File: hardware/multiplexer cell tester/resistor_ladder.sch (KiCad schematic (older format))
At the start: 27 parts, among them U10 ADG841YKSZ-500RL7, U11 ADG841YKSZ-500RL7, U12 ADG841YKSZ-500RL7, U13 74HC590, U13 ADG841YKSZ-500RL7, U6 ADG841YKSZ-500RL7, U7 ADG841YKSZ-500RL7, U8 ADG841YKSZ-500RL7, U9 ADG841YKSZ-500RL7

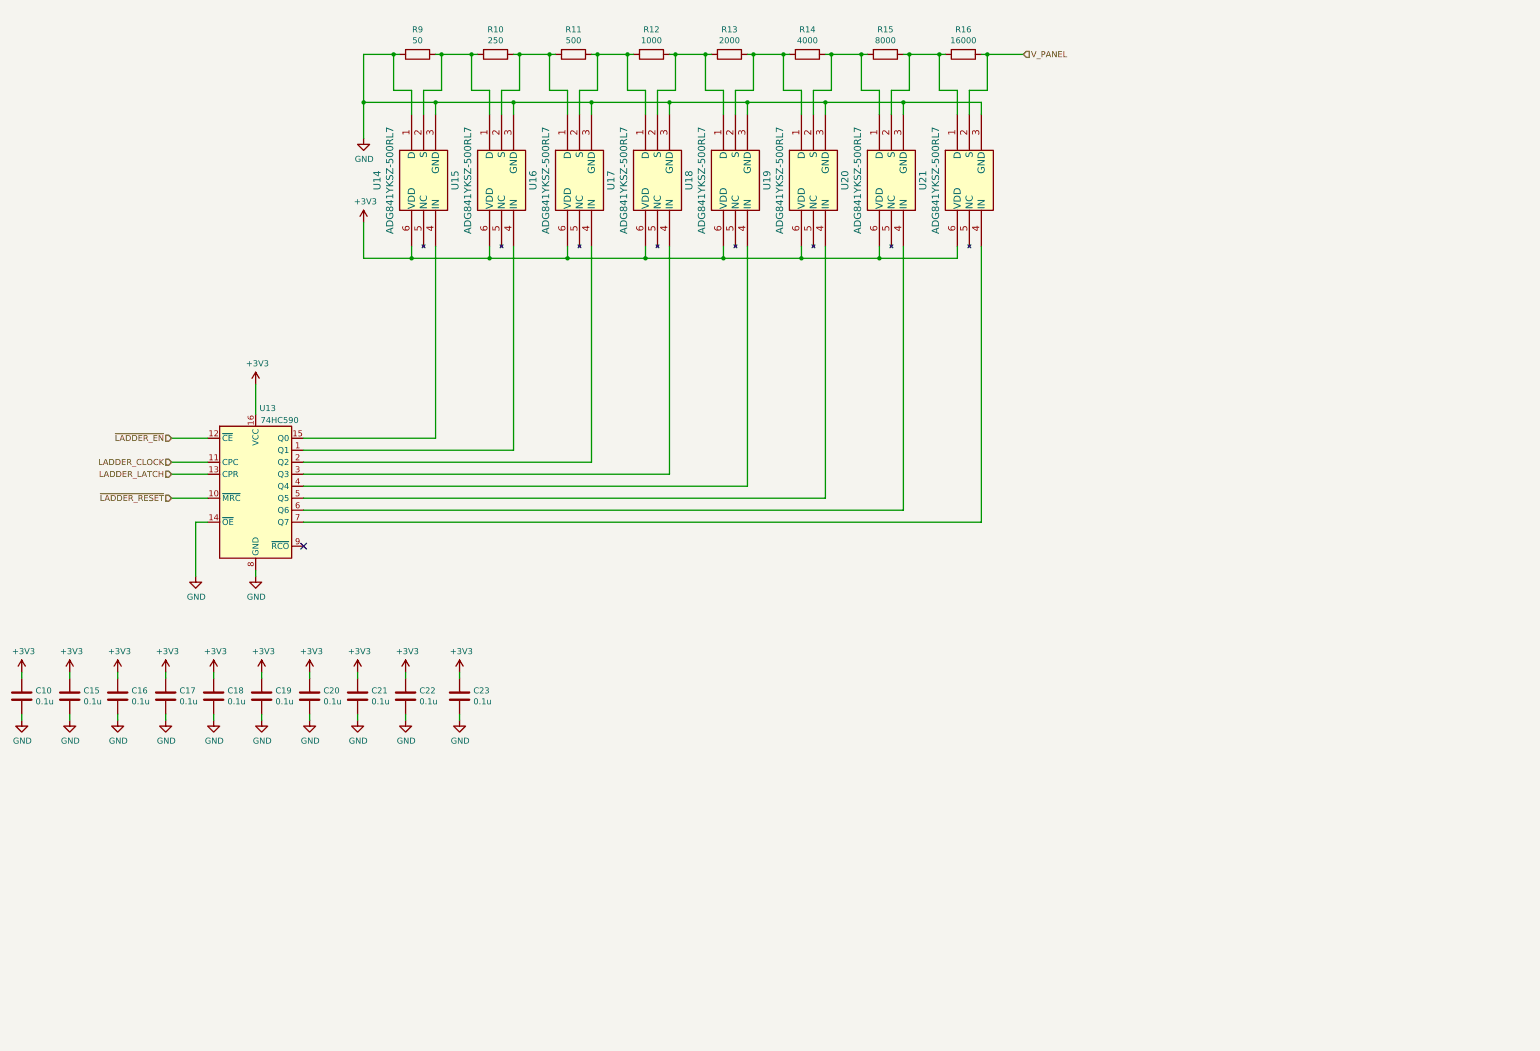
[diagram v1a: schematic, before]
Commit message: Finalized curve tracer
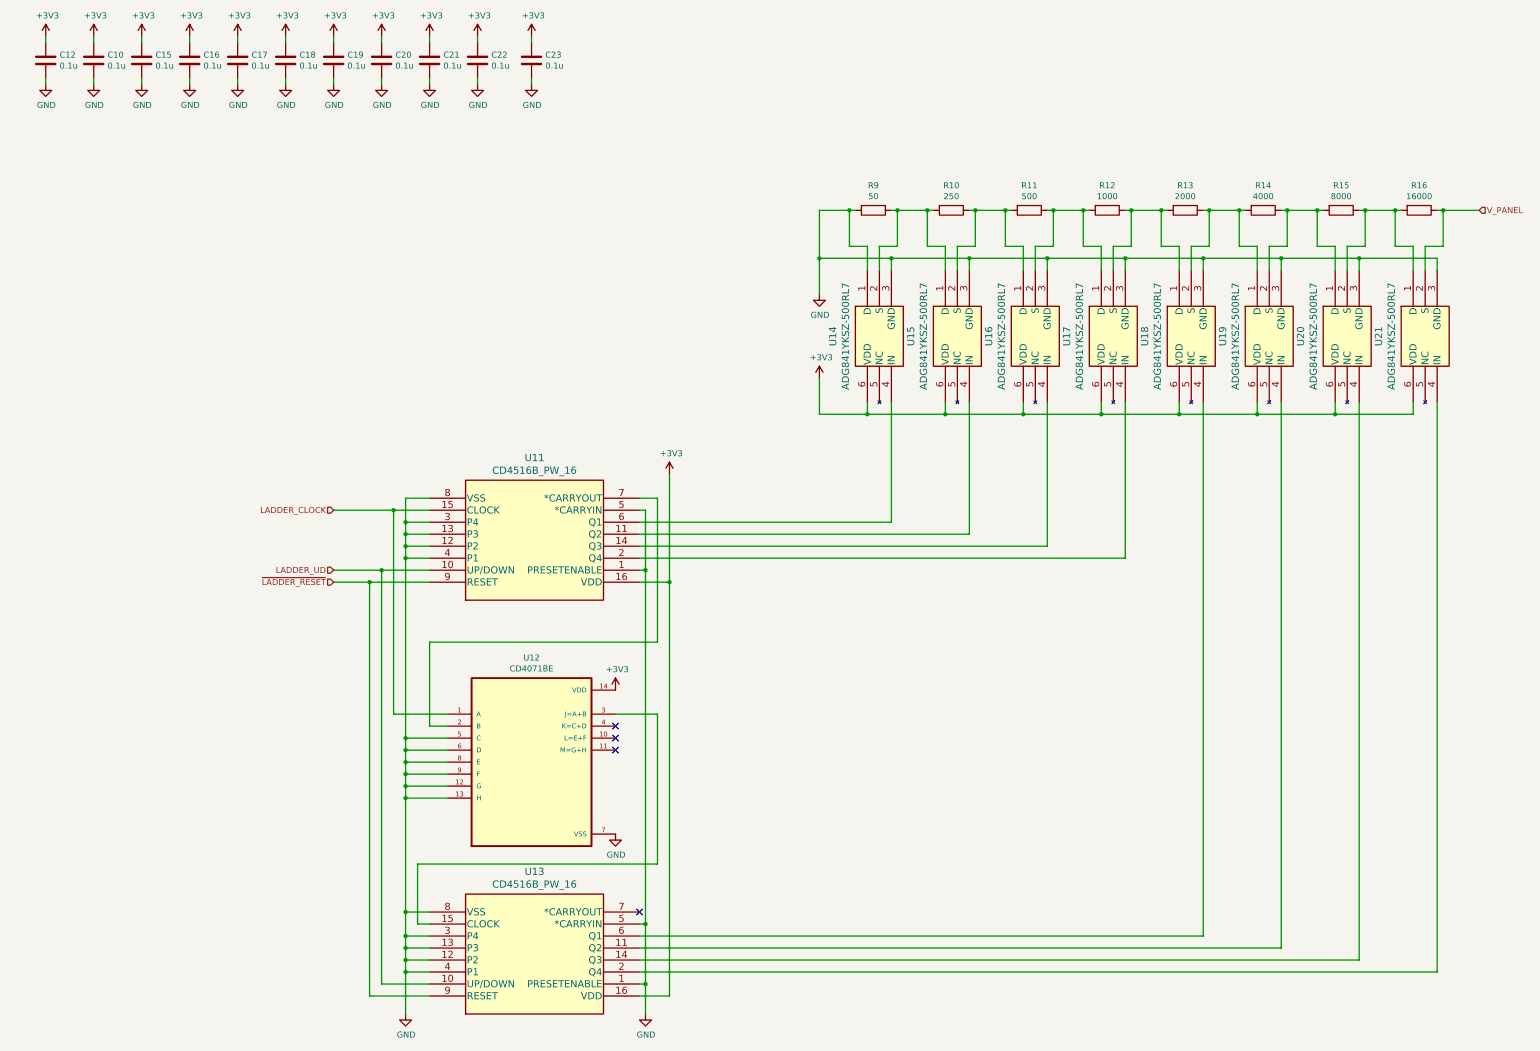
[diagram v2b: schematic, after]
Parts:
- removed U13: 74HC590, Package_SO:SOIC-16_3.9x9.9mm_P1.27mm, symbol 74xx:74HC590
- added C12: 0.1u, Capacitor_SMD:C_0603_1608Metric, symbol Device:C
- added U11, U13: CD4516B_PW_16, Package_SO:TSSOP-16_4.4x5mm_P0.65mm, symbol CD4516BPWR:CD4516B_PW_16
- added U12: CD4071BE, Package_SO:TSSOP-14_4.4x5mm_P0.65mm, symbol CD4071BE:CD4071BE
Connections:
- net +3V3: now also C12.1, U11.16 (VDD), U12.14 (VDD), U13.16 (VDD)
- net GND: now also C12.2, U11.1 (PRESETENABLE), U11.12 (P2), U11.13 (P3), U11.3 (P4), U11.4 (P1), U11.5 (*CARRYIN), U11.8 (VSS), U12.12 (G), U12.13 (H), U12.5 (C), U12.6 (D), U12.7 (VSS), U12.8 (E), U12.9 (F), U13.1 (PRESETENABLE), U13.12 (P2), U13.13 (P3), U13.3 (P4), U13.4 (P1), U13.5 (*CARRYIN), U13.8 (VSS)
- net LADDER_CLOCK: now also U11.15 (CLOCK), U12.1 (A)
- net ~LADDER_RESET: now also U11.9 (RESET), U13.9 (RESET)
- net at U8.4 (IN): now also U11.14 (Q3)
- net at U9.4 (IN): now also U11.2 (Q4)
- net at U10.4 (IN): now also U13.6 (Q1)
- net at U11.4 (IN): now also U13.11 (Q2)
- net at U12.4 (IN): now also U13.14 (Q3)
- net at U13.4 (IN): now also U13.2 (Q4)
- net at U7.4 (IN): now also U11.11 (Q2)
- net at U6.4 (IN): now also U11.6 (Q1)
- new net: U12.3 (J=A+B), U13.15 (CLOCK)
- new net: U11.7 (*CARRYOUT), U12.2 (B)
- new net LADDER_UD: U11.10 (UP/DOWN), U13.10 (UP/DOWN)
- no-connect marks 1 -> 4
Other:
- moved on the sheet: C10, C15, C16, C17, C18, C19, C20, C21, C22, C23, R10, R11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
